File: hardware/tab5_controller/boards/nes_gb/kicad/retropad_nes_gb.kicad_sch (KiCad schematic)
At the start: 25 parts, among them J1 Tab5 Ext.Port1, J2 UPDI, SW1 UP, SW2 DOWN, SW3 LEFT, SW4 RIGHT, SW5 B, SW6 A, SW7 SELECT, SW8 START, SW9 MENU, U1 AVR32DD28-I/SO

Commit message: tab5_controller: merge the NES and Game Boy boards into one
The two boards had the same buttons, pins and host mapping; only A/B
placement and the console ID differed. The new nes_gb board replaces
both:

- A sits 4 mm above B (16 mm apart), between the NES pad's level
  buttons and the Game Boy's diagonal.
- It reports console ID 1 ("NES / Game Boy"). layout.ALIASES keeps
  ID 2 mapped identically in pinmap.h, so a GB-strapped board still
  works; the pin tables are unchanged.
- Routed with Freerouting 1.9: DRC 0 unconnected (silkscreen warnings
  only), schematic vs PCB 0 differences, switches on the pins pinmap.h
  expects. Host test passes.

Co-Authored-By: Claude Opus 5.5 <noreply@anthropic.com>
Claude-Session: https://claude.ai/code/session_01NhSHTsezreiVZCnuBhQzP2
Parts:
- R6: value DNP -> 0R; now fitted; now in the parts list
- R7: value 0R -> DNP; now not fitted; now left out of the parts list
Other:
- note added: "Console ID straps: 0R to GND = bit set. NES / Game Boy = ID 1 (fit R6; R7, R8, R9 DNP)"
- note removed: "Console ID straps: 0R to GND = bit set. Game Boy = ID 2 (fit R7; R6, R8, R9 DNP)"
- title: RetroPad Game Boy controller (console ID 2) -> RetroPad NES / Game Boy controller (console ID 1)

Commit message: tab5_controller: 0805 hand-solder passives on every board
Swap the 0603 resistors and capacitors (decoupling, I2C pull-ups, reset
pull-up, console-ID straps) for KiCad's 0805 HandSolder footprints, which
have longer pads for soldering by hand. C2 turns 90 degrees so its larger
courtyard clears U1. All four boards are re-routed with Freerouting 1.9;
schematics, BOMs, DRC reports and renders are regenerated.

DRC: 0 errors and 0 unconnected pads on every board (silkscreen and
library-path warnings only). Schematic vs PCB: 0 differences.

Co-Authored-By: Claude Opus 5.5 <noreply@anthropic.com>
Claude-Session: https://claude.ai/code/session_016pgTnJvu7Wh4anaUwDfFmN
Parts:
- C1, C2, C3, C4: footprint Capacitor_SMD:C_0603_1608Metric -> Capacitor_SMD:C_0805_2012Metric_Pad1.18x1.45mm_HandSolder
- R1, R2, R3, R6, R7, R8, R9: footprint Resistor_SMD:R_0603_1608Metric -> Resistor_SMD:R_0805_2012Metric_Pad1.20x1.40mm_HandSolder
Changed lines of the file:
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@@
     (property
       "Footprint"
-      "Capacitor_SMD:C_0603_1608Metric"
+      "Capacitor_SMD:C_0805_2012Metric_Pad1.18x1.45mm_HandSolder"
       (at 160.02 129.54 0)
       (effects (font (size 1.27 1.27)) hide))
@@
     (property
       "Footprint"
-      "Capacitor_SMD:C_0603_1608Metric"
+      "Capacitor_SMD:C_0805_2012Metric_Pad1.18x1.45mm_HandSolder"
       (at 175.26 129.54 0)
       (effects (font (size 1.27 1.27)) hide))
@@
     (property
       "Footprint"
-      "Capacitor_SMD:C_0603_1608Metric"
+      "Capacitor_SMD:C_0805_2012Metric_Pad1.18x1.45mm_HandSolder"
       (at 190.5 129.54 0)
       (effects (font (size 1.27 1.27)) hide))
@@
     (property
       "Footprint"
-      "Capacitor_SMD:C_0603_1608Metric"
+      "Capacitor_SMD:C_0805_2012Metric_Pad1.18x1.45mm_HandSolder"
       (at 204.47 129.54 0)
       (effects (font (size 1.27 1.27)) hide))
@@
     (property
       "Footprint"
-      "Resistor_SMD:R_0603_1608Metric"
+      "Resistor_SMD:R_0805_2012Metric_Pad1.20x1.40mm_HandSolder"
       (at 160.02 154.94 0)
       (effects (font (size 1.27 1.27)) hide))
@@
     (property
       "Footprint"
-      "Resistor_SMD:R_0603_1608Metric"
+      "Resistor_SMD:R_0805_2012Metric_Pad1.20x1.40mm_HandSolder"
       (at 175.26 154.94 0)
       (effects (font (size 1.27 1.27)) hide))
@@
     (property
       "Footprint"
-      "Resistor_SMD:R_0603_1608Metric"
+      "Resistor_SMD:R_0805_2012Metric_Pad1.20x1.40mm_HandSolder"
       (at 190.5 154.94 0)
       (effects (font (size 1.27 1.27)) hide))
@@
     (property
       "Footprint"
-      "Resistor_SMD:R_0603_1608Metric"
+      "Resistor_SMD:R_0805_2012Metric_Pad1.20x1.40mm_HandSolder"
       (at 160.02 190.5 0)
       (effects (font (size 1.27 1.27)) hide))
@@
     (property
       "Footprint"
-      "Resistor_SMD:R_0603_1608Metric"
+      "Resistor_SMD:R_0805_2012Metric_Pad1.20x1.40mm_HandSolder"
       (at 175.26 190.5 0)
       (effects (font (size 1.27 1.27)) hide))
@@
     (property
       "Footprint"
-      "Resistor_SMD:R_0603_1608Metric"
+      "Resistor_SMD:R_0805_2012Metric_Pad1.20x1.40mm_HandSolder"
       (at 190.5 190.5 0)
       (effects (font (size 1.27 1.27)) hide))
@@
     (property
       "Footprint"
-      "Resistor_SMD:R_0603_1608Metric"
+      "Resistor_SMD:R_0805_2012Metric_Pad1.20x1.40mm_HandSolder"
       (at 204.47 190.5 0)
       (effects (font (size 1.27 1.27)) hide))

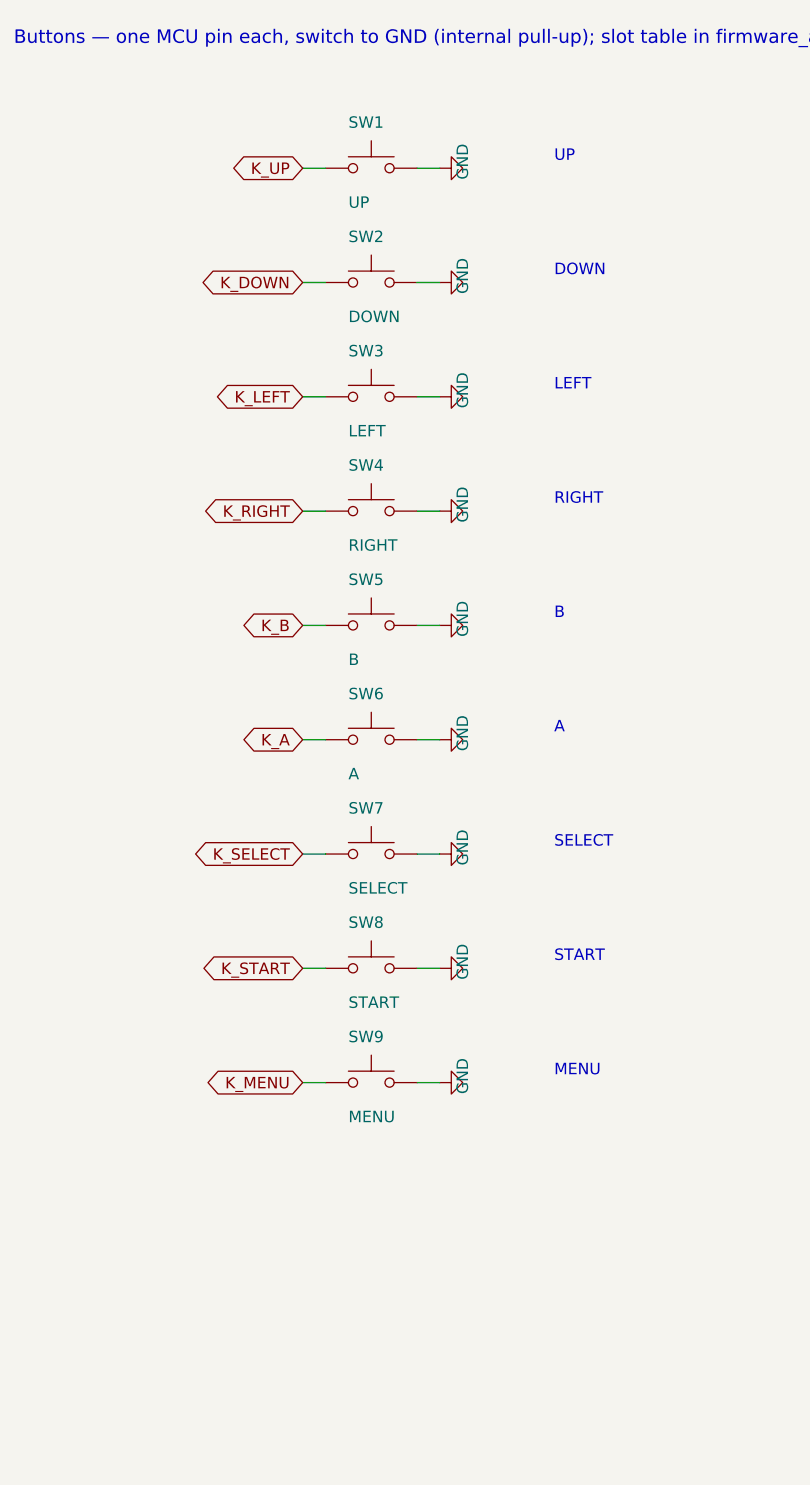
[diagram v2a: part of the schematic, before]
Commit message: tab5_controller: 4-pin tact switch symbols and footprints
The 6x6 and 12x12 switches are 4-leg parts, and the production layout in
EasyEDA uses their 4-pin symbols, so the KiCad boards now match:

- kicad_lib/RetroPad.pretty: SW_PUSH_6mm_4pin and SW_PUSH-12mm_4pin,
  KiCad's footprints with the pads renumbered 1-4 (pad 1 top-left, then
  clockwise; tied pairs 1-2 and 3-4, the legs 6.5 / 12.5 mm apart).
  gen_pcb.py writes them from the stock footprints and points each
  board's fp-lib-table at the library.
- RetroPad:SW_Push_4pin symbol in gen_sch.py: 1-2 tied, 4-3 tied, one
  contact between. KiCad's 4-pin SW_Push_Dual is a two-contact switch,
  so it doesn't fit these parts.
- Wiring: legs 1-2 to GND, 3-4 to K_<button>. L/R (right angle, two
  contacts plus mounting legs) keep the 2-pin SW_Push.
- All four boards re-routed: DRC 0 unconnected (silkscreen warnings
  only), schematic vs PCB 0 differences, every switch on the pin
  pinmap.h expects; firmware host test passes; Gerber/drill export OK.

Co-Authored-By: Claude Opus 5.5 <noreply@anthropic.com>
Claude-Session: https://claude.ai/code/session_01NhSHTsezreiVZCnuBhQzP2
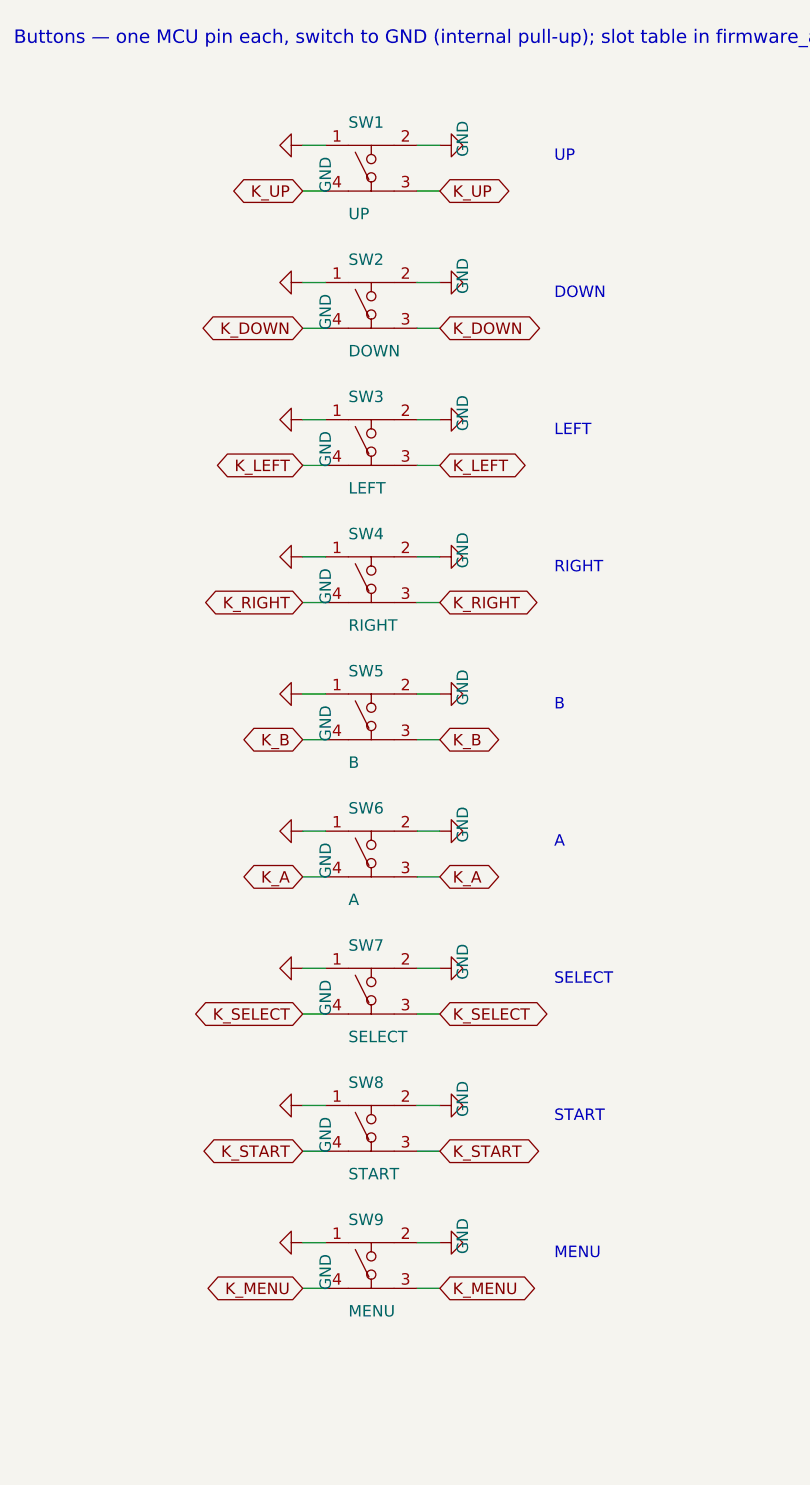
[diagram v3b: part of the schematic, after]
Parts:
- SW1, SW2, SW3, SW4, SW7, SW8, SW9: footprint Button_Switch_THT:SW_PUSH_6mm -> RetroPad:SW_PUSH_6mm_4pin; symbol Switch:SW_Push -> RetroPad:SW_Push_4pin
- SW5, SW6: footprint Button_Switch_THT:SW_PUSH-12mm -> RetroPad:SW_PUSH-12mm_4pin; symbol Switch:SW_Push -> RetroPad:SW_Push_4pin
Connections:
- net GND: now also SW1.1, SW2.1, SW3.1, SW4.1, SW5.1, SW6.1, SW7.1, SW8.1, SW9.1
- net K_A: now also SW6.3, SW6.4; no longer SW6.1
- net K_B: now also SW5.3, SW5.4; no longer SW5.1
- net K_DOWN: now also SW2.3, SW2.4; no longer SW2.1
- net K_LEFT: now also SW3.3, SW3.4; no longer SW3.1
- net K_MENU: now also SW9.3, SW9.4; no longer SW9.1
- net K_RIGHT: now also SW4.3, SW4.4; no longer SW4.1
- net K_SELECT: now also SW7.3, SW7.4; no longer SW7.1
- net K_START: now also SW8.3, SW8.4; no longer SW8.1
- net K_UP: now also SW1.3, SW1.4; no longer SW1.1
